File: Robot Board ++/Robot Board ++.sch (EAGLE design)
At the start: 123 parts, among them U10 74LVTH125.RGY, U11 SCHA4B0400, U12 BLUETOOTH-RN41", U13 XBEE-1XBEE-1_LOCK, U5 TPS5331[8/9].DQP, U6 TPS62082.DSG, U7 PCA9557.RGV, U8 MPU-6050

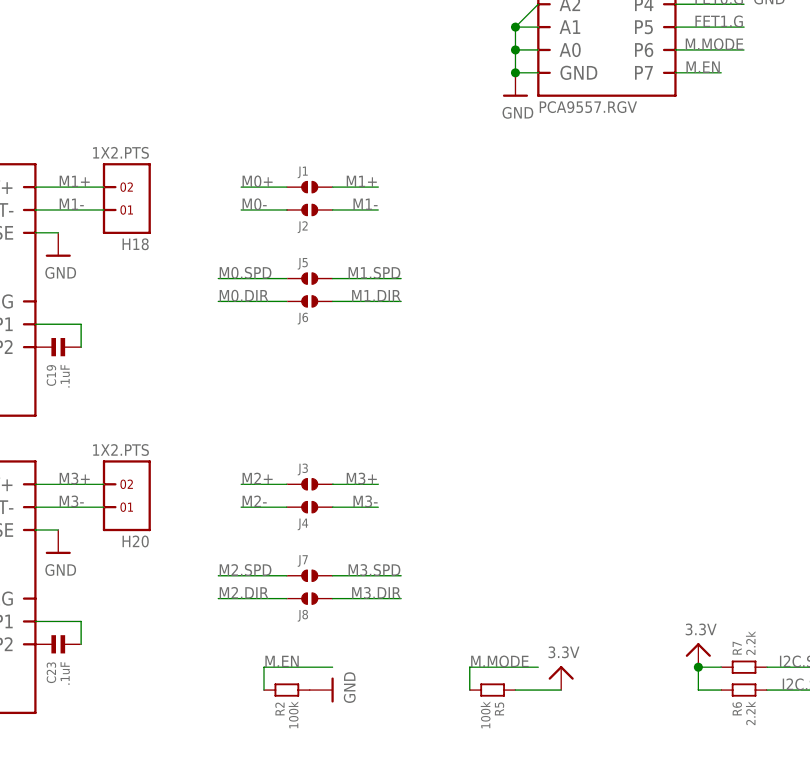
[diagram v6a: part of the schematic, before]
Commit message: Removed SMD jumpers for Motors. Will put onto adapter instead. Layout and silkscreen on board tenatively completed. Schematic will be cleaned up after Senior design paper due tomorrow.
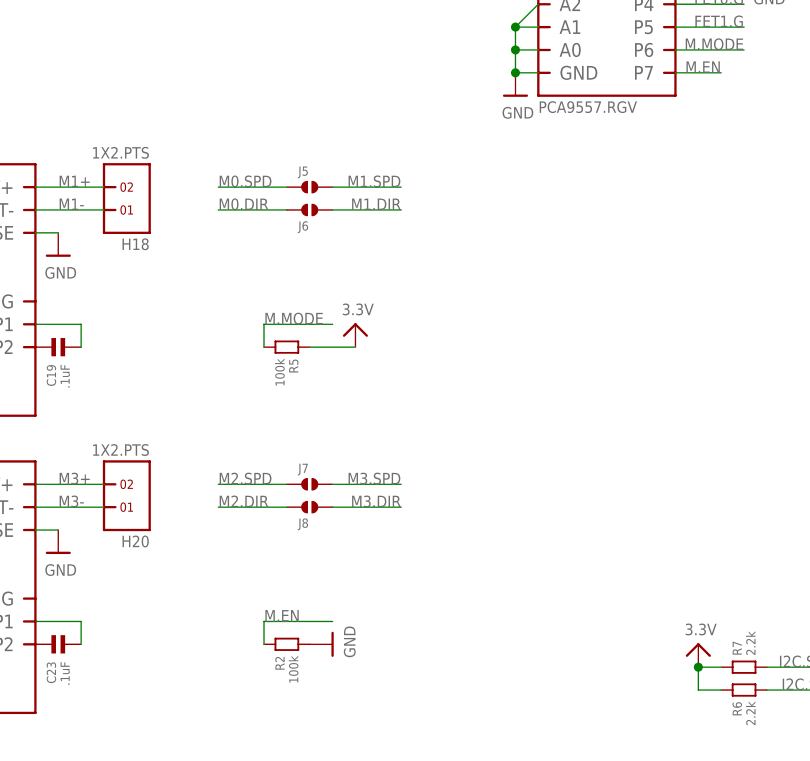
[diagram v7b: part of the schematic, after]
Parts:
- removed J1, J2, J3, J4: (no value), solderjumper:SOLDERJUMPER.2.XL
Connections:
- net M0+: no longer J1.1
- net M0-: no longer J2.1
- net M1+: no longer J1.2
- net M1-: no longer J2.2
- net M2+: no longer J3.1
- net M2-: no longer J4.1
- net M3+: no longer J3.2
- net M3-: no longer J4.2
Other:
- moved on the sheet: J5, J6, J7, J8, R2, R5
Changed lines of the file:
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@@
 <part name="C30" library="standardparts" deviceset="CAPACITOR" device=".0603" value=".1uF"/>
 <part name="C31" library="standardparts" deviceset="CAPACITOR" device=".0603" value=".1uF"/>
-<part name="J1" library="solderjumper" deviceset="SOLDERJUMPER.2" device=".XL"/>
-<part name="J2" library="solderjumper" deviceset="SOLDERJUMPER.2" device=".XL"/>
-<part name="J3" library="solderjumper" deviceset="SOLDERJUMPER.2" device=".XL"/>
-<part name="J4" library="solderjumper" deviceset="SOLDERJUMPER.2" device=".XL"/>
 <part name="J5" library="solderjumper" deviceset="SOLDERJUMPER.2" device=".LRG"/>
 <part name="J6" library="solderjumper" deviceset="SOLDERJUMPER.2" device=".LRG"/>
@@
 <instance part="C8" gate="G$1" x="139.7" y="228.6" rot="MR270"/>
 <instance part="C15" gate="G$1" x="142.24" y="228.6" rot="R270"/>
-<instance part="R2" gate="G$1" x="134.62" y="10.16" rot="MR180"/>
-<instance part="U$106" gate="G$1" x="139.7" y="10.16" rot="R90"/>
+<instance part="R2" gate="G$1" x="134.62" y="15.24" rot="MR180"/>
+<instance part="U$106" gate="G$1" x="139.7" y="15.24" rot="R90"/>
 <instance part="H22" gate="G$1" x="220.98" y="17.78"/>
 <instance part="U$108" gate="G$1" x="226.06" y="20.32"/>
@@
 <instance part="C30" gate="G$1" x="55.88" y="30.48" rot="MR270"/>
 <instance part="C31" gate="G$1" x="71.12" y="30.48" rot="R270"/>
-<instance part="J1" gate="G$1" x="137.16" y="66.04"/>
-<instance part="J2" gate="G$1" x="137.16" y="63.5" rot="MR180"/>
-<instance part="J3" gate="G$1" x="137.16" y="33.02"/>
-<instance part="J4" gate="G$1" x="137.16" y="30.48" rot="MR180"/>
-<instance part="J5" gate="G$1" x="137.16" y="55.88"/>
-<instance part="J6" gate="G$1" x="137.16" y="53.34" rot="MR180"/>
-<instance part="J7" gate="G$1" x="137.16" y="22.86"/>
-<instance part="J8" gate="G$1" x="137.16" y="20.32" rot="MR180"/>
+<instance part="J5" gate="G$1" x="137.16" y="66.04"/>
+<instance part="J6" gate="G$1" x="137.16" y="63.5" rot="MR180"/>
+<instance part="J7" gate="G$1" x="137.16" y="33.02"/>
+<instance part="J8" gate="G$1" x="137.16" y="30.48" rot="MR180"/>
 <instance part="C16" gate="G$1" x="60.96" y="60.96"/>
 <instance part="C18" gate="G$1" x="60.96" y="27.94"/>
@@
 <instance part="U$136" gate="G$1" x="274.32" y="12.7"/>
 <instance part="U$56" gate="G$1" x="347.98" y="88.9"/>
-<instance part="R5" gate="G$1" x="157.48" y="10.16" rot="R180"/>
+<instance part="R5" gate="G$1" x="134.62" y="48.26" rot="R180"/>
 <instance part="U$111" gate="G$1" x="340.36" y="198.12"/>
 <instance part="U$137" gate="G$1" x="340.36" y="187.96"/>
@@
 <instance part="U$37" gate="G$1" x="63.5" y="96.52"/>
 <instance part="U$38" gate="G$1" x="63.5" y="114.3"/>
-<instance part="U$39" gate="G$1" x="165.1" y="12.7"/>
+<instance part="U$39" gate="G$1" x="142.24" y="50.8"/>
 </instances>
 <busses>
@@
 <segment>
 <pinref part="R5" gate="G$1" pin="1"/>
-<wire x1="160.02" y1="10.16" x2="165.1" y2="10.16" width="0.1524" layer="91"/>
+<wire x1="137.16" y1="48.26" x2="142.24" y2="48.26" width="0.1524" layer="91"/>
 <pinref part="U$39" gate="G$1" pin="3.3V"/>
 </segment>
@@
 <label x="17.78" y="30.48" size="1.27" layer="95" rot="MR0"/>
 </segment>
-<segment>
-<pinref part="J4" gate="G$1" pin="1"/>
-<wire x1="134.62" y1="30.48" x2="129.54" y2="30.48" width="0.1524" layer="91"/>
-<label x="129.54" y="30.48" size="1.27" layer="95"/>
-</segment>
 </net>
 <net name="M2+" class="0">
@@
 <label x="17.78" y="33.02" size="1.27" layer="95" rot="MR0"/>
 </segment>
-<segment>
-<pinref part="J3" gate="G$1" pin="1"/>
-<wire x1="129.54" y1="33.02" x2="134.62" y2="33.02" width="0.1524" layer="91"/>
-<label x="129.54" y="33.02" size="1.27" layer="95"/>
-</segment>
 </net>
 <net name="M0-" class="0">
@@
 <label x="17.78" y="63.5" size="1.27" layer="95" rot="MR0"/>
 </segment>
-<segment>
-<pinref part="J2" gate="G$1" pin="1"/>
-<wire x1="134.62" y1="63.5" x2="129.54" y2="63.5" width="0.1524" layer="91"/>
-<label x="129.54" y="63.5" size="1.27" layer="95"/>
-</segment>
 </net>
 <net name="M0+" class="0">
@@
 <label x="17.78" y="66.04" size="1.27" layer="95" rot="MR0"/>
 </segment>
-<segment>
-<pinref part="J1" gate="G$1" pin="1"/>
-<wire x1="129.54" y1="66.04" x2="134.62" y2="66.04" width="0.1524" layer="91"/>
-<label x="129.54" y="66.04" size="1.27" layer="95"/>
-</segment>
 </net>
 <net name="M1+" class="0">
@@
 <label x="109.22" y="66.04" size="1.27" layer="95"/>
 </segment>
-<segment>
-<pinref part="J1" gate="G$1" pin="2"/>
-<wire x1="139.7" y1="66.04" x2="144.78" y2="66.04" width="0.1524" layer="91"/>
-<label x="144.78" y="66.04" size="1.27" layer="95" rot="MR0"/>
-</segment>
 </net>
 <net name="M1-" class="0">
@@
 <label x="109.22" y="63.5" size="1.27" layer="95"/>
 </segment>
-<segment>
-<pinref part="J2" gate="G$1" pin="2"/>
-<wire x1="144.78" y1="63.5" x2="139.7" y2="63.5" width="0.1524" layer="91"/>
-<label x="144.78" y="63.5" size="1.27" layer="95" rot="MR0"/>
-</segment>
 </net>
 <net name="M3+" class="0">
@@
 <label x="109.22" y="33.02" size="1.27" layer="95"/>
 </segment>
-<segment>
-<pinref part="J3" gate="G$1" pin="2"/>
-<wire x1="139.7" y1="33.02" x2="144.78" y2="33.02" width="0.1524" layer="91"/>
-<label x="144.78" y="33.02" size="1.27" layer="95" rot="MR0"/>
-</segment>
 </net>
 <net name="M3-" class="0">
@@
 <label x="109.22" y="30.48" size="1.27" layer="95"/>
 </segment>
-<segment>
-<pinref part="J4" gate="G$1" pin="2"/>
-<wire x1="144.78" y1="30.48" x2="139.7" y2="30.48" width="0.1524" layer="91"/>
-<label x="144.78" y="30.48" size="1.27" layer="95" rot="MR0"/>
-</segment>
 </net>
 <net name="M.EN" class="0">
@@
 </segment>
 <segment>
-<wire x1="132.08" y1="12.7" x2="132.08" y2="10.16" width="0.1524" layer="91"/>
+<wire x1="132.08" y1="17.78" x2="132.08" y2="15.24" width="0.1524" layer="91"/>
 <pinref part="R2" gate="G$1" pin="1"/>
-<label x="132.08" y="12.7" size="1.27" layer="95"/>
-<wire x1="132.08" y1="12.7" x2="139.7" y2="12.7" width="0.1524" layer="91"/>
+<label x="132.08" y="17.78" size="1.27" layer="95"/>
+<wire x1="132.08" y1="17.78" x2="139.7" y2="17.78" width="0.1524" layer="91"/>
 </segment>
 <segment>
@@
 <segment>
 <pinref part="J5" gate="G$1" pin="1"/>
-<wire x1="134.62" y1="55.88" x2="127" y2="55.88" width="0.1524" layer="91"/>
-<label x="127" y="55.88" size="1.27" layer="95"/>
+<wire x1="134.62" y1="66.04" x2="127" y2="66.04" width="0.1524" layer="91"/>
+<label x="127" y="66.04" size="1.27" layer="95"/>
 </segment>
 </net>
@@
 <segment>
 <pinref part="J6" gate="G$1" pin="1"/>
-<wire x1="127" y1="53.34" x2="134.62" y2="53.34" width="0.1524" layer="91"/>
-<label x="127" y="53.34" size="1.27" layer="95"/>
+<wire x1="127" y1="63.5" x2="134.62" y2="63.5" width="0.1524" layer="91"/>
+<label x="127" y="63.5" size="1.27" layer="95"/>
 </segment>
 <segment>
@@
 <segment>
 <pinref part="J7" gate="G$1" pin="1"/>
-<wire x1="134.62" y1="22.86" x2="127" y2="22.86" width="0.1524" layer="91"/>
-<label x="127" y="22.86" size="1.27" layer="95"/>
+<wire x1="134.62" y1="33.02" x2="127" y2="33.02" width="0.1524" layer="91"/>
+<label x="127" y="33.02" size="1.27" layer="95"/>
 </segment>
 </net>
@@
 <segment>
 <pinref part="J8" gate="G$1" pin="1"/>
-<wire x1="127" y1="20.32" x2="134.62" y2="20.32" width="0.1524" layer="91"/>
-<label x="127" y="20.32" size="1.27" layer="95"/>
+<wire x1="127" y1="30.48" x2="134.62" y2="30.48" width="0.1524" layer="91"/>
+<label x="127" y="30.48" size="1.27" layer="95"/>
 </segment>
 <segment>
@@
 </segment>
 <segment>
-<wire x1="162.56" y1="12.7" x2="154.94" y2="12.7" width="0.1524" layer="91"/>
-<wire x1="154.94" y1="12.7" x2="154.94" y2="10.16" width="0.1524" layer="91"/>
+<wire x1="139.7" y1="50.8" x2="132.08" y2="50.8" width="0.1524" layer="91"/>
+<wire x1="132.08" y1="50.8" x2="132.08" y2="48.26" width="0.1524" layer="91"/>
 <pinref part="R5" gate="G$1" pin="2"/>
-<label x="154.94" y="12.7" size="1.27" layer="95"/>
+<label x="132.08" y="50.8" size="1.27" layer="95"/>
 </segment>
 <segment>
@@
 <segment>
 <pinref part="J8" gate="G$1" pin="2"/>
-<wire x1="139.7" y1="20.32" x2="147.32" y2="20.32" width="0.1524" layer="91"/>
-<label x="147.32" y="20.32" size="1.27" layer="95" rot="MR0"/>
+<wire x1="139.7" y1="30.48" x2="147.32" y2="30.48" width="0.1524" layer="91"/>
+<label x="147.32" y="30.48" size="1.27" layer="95" rot="MR0"/>
 </segment>
 <segment>
@@
 <segment>
 <pinref part="J7" gate="G$1" pin="2"/>
-<wire x1="147.32" y1="22.86" x2="139.7" y2="22.86" width="0.1524" layer="91"/>
-<label x="147.32" y="22.86" size="1.27" layer="95" rot="MR0"/>
+<wire x1="147.32" y1="33.02" x2="139.7" y2="33.02" width="0.1524" layer="91"/>
+<label x="147.32" y="33.02" size="1.27" layer="95" rot="MR0"/>
 </segment>
 </net>
@@
 <segment>
 <pinref part="J6" gate="G$1" pin="2"/>
-<wire x1="139.7" y1="53.34" x2="147.32" y2="53.34" width="0.1524" layer="91"/>
-<label x="147.32" y="53.34" size="1.27" layer="95" rot="MR0"/>
+<wire x1="139.7" y1="63.5" x2="147.32" y2="63.5" width="0.1524" layer="91"/>
+<label x="147.32" y="63.5" size="1.27" layer="95" rot="MR0"/>
 </segment>
 <segment>
@@
 <segment>
 <pinref part="J5" gate="G$1" pin="2"/>
-<wire x1="147.32" y1="55.88" x2="139.7" y2="55.88" width="0.1524" layer="91"/>
-<label x="147.32" y="55.88" size="1.27" layer="95" rot="MR0"/>
-</segment>
-</net>
+<wire x1="147.32" y1="66.04" x2="139.7" y2="66.04" width="0.1524" layer="91"/>
+<label x="147.32" y="66.04" size="1.27" layer="95" rot="MR0"/>
+</segment>
+</net>

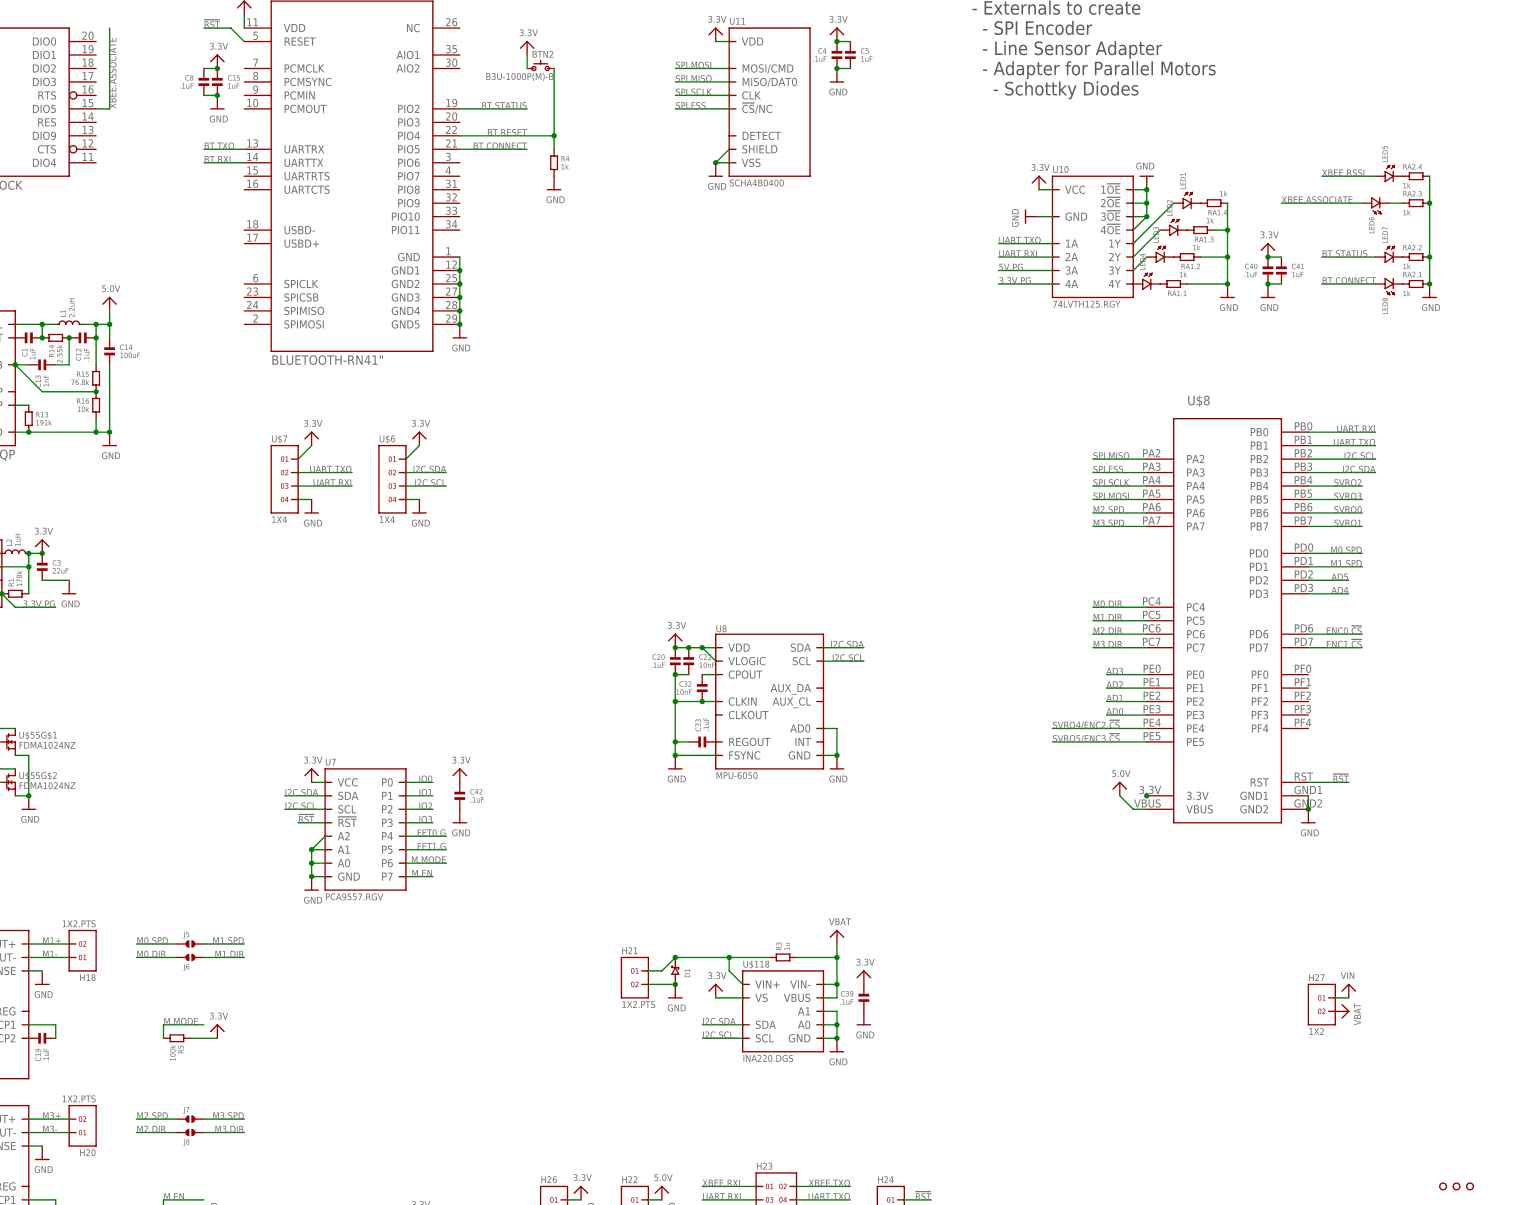
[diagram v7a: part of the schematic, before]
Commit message: Modified Schematic. Will need to be cleaned up. Added two ICs to look into (SPI Stereo DAC & Audio Amp)
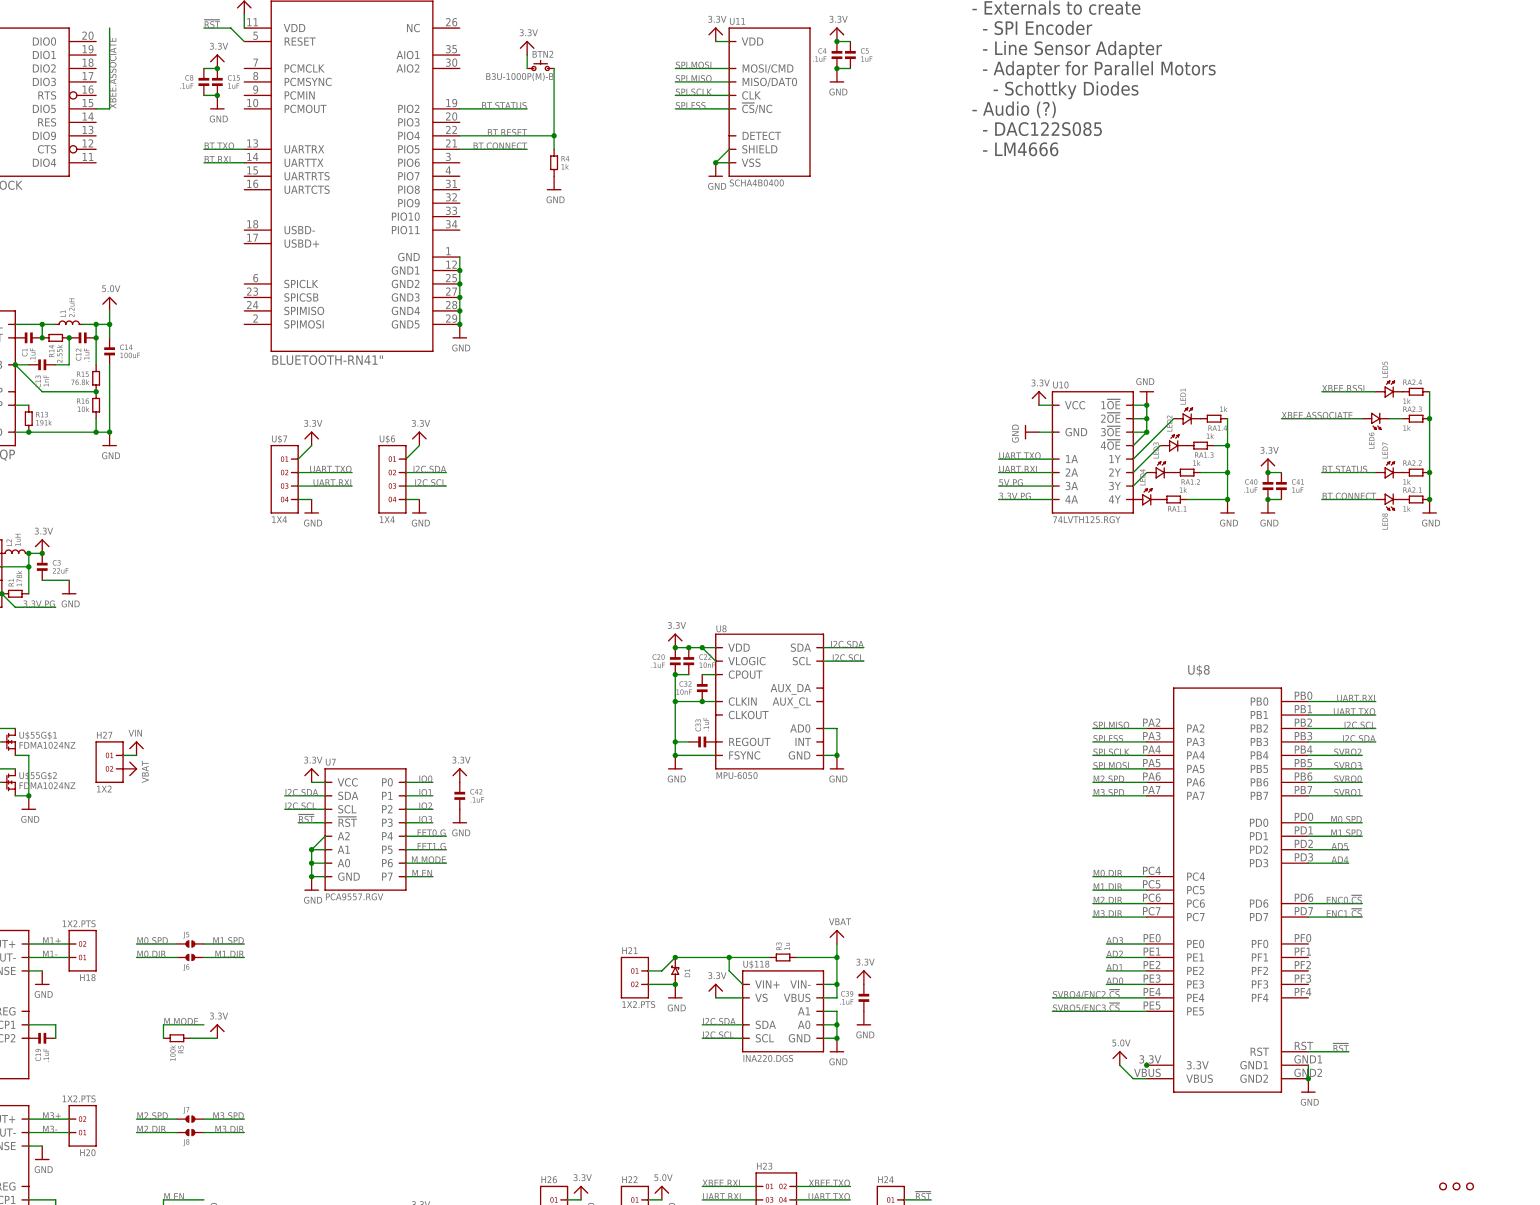
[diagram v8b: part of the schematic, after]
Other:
- note added: "NOTES: - Remove R9 & R10 to decouple B[6/7] from D[0/1] - Externals to create - SPI Encoder - Line Sensor Adapter - Adapter for Parallel Motors - Schottky Diodes - Audio (?) - DAC122S085 - LM4666"
- note removed: "NOTES: - Remove R9 & R10 to decouple B[6/7] from D[0/1] - Externals to create - SPI Encoder - Line Sensor Adapter - Adapter for Parallel Motors - Schottky Diodes"
- moved on the sheet: C40, C41, H27, LED1, LED2, LED3, LED4, LED5, LED6, LED7, LED8, RA1.1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
